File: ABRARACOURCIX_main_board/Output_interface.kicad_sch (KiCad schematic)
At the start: 1 part

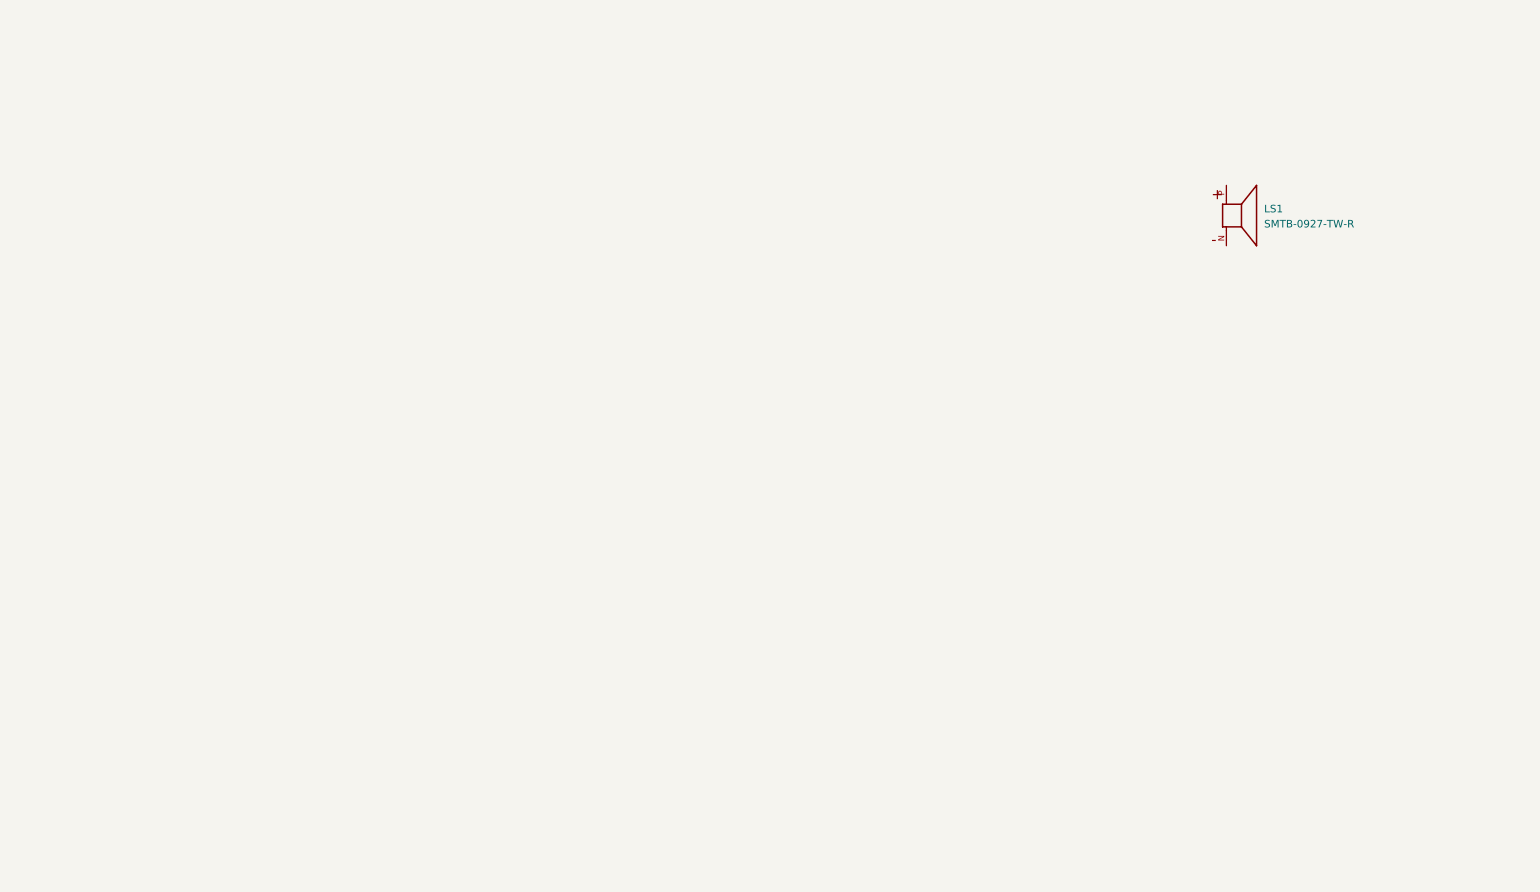
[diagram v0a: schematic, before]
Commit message: Terminé les interconnects
Toutes les interfaces et le power sont terminés. (À vérifier)
Reste à ajouter toutes les connexions au ICM et stm32
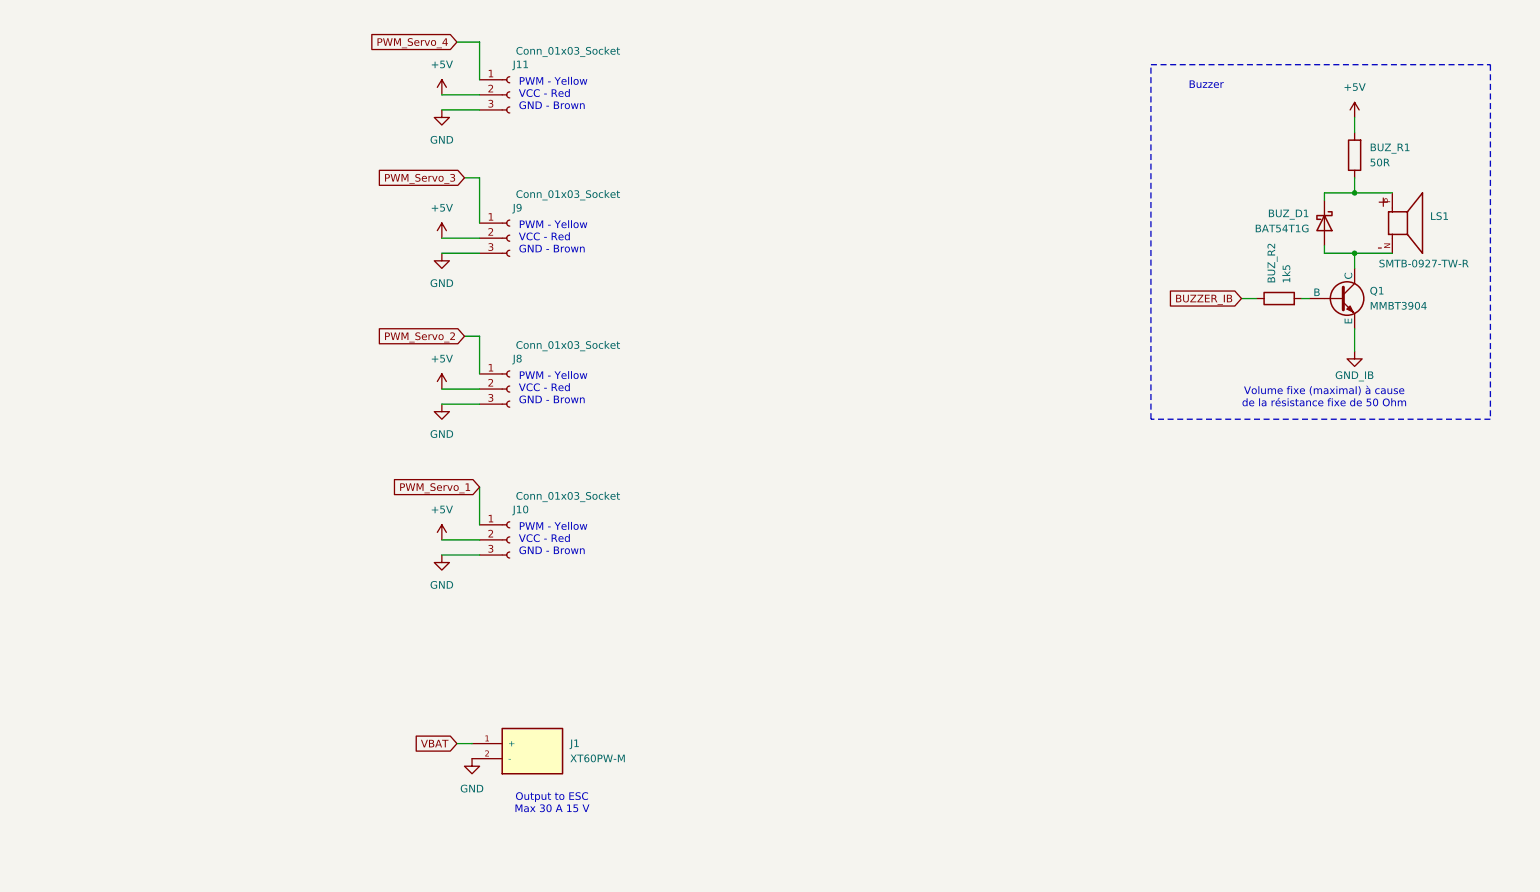
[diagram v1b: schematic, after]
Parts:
- added BUZ_D1: BAT54T1G, Diode_SMD:D_SOD-123, symbol Diode:1N6858UR
- added BUZ_R1: 50R, Resistor_SMD:R_1206_3216Metric, symbol Device:R
- added BUZ_R2: 1k5, Resistor_SMD:R_1206_3216Metric, symbol Device:R
- added J1: XT60PW-M, XT60PW-M:AMASS_XT60PW-M, symbol GAUL_ABRARACOURCIX:XT60PW-M
- added J10, J11, J8, J9: Conn_01x03_Socket, symbol Connector:Conn_01x03_Socket
- added Q1: MMBT3904, Footprints:SOT-23, symbol Simulation_SPICE:NPN
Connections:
- net at LS1.N: now also BUZ_D1.2 (A), Q1.1 (C)
- net at LS1.P: now also BUZ_D1.1 (K), BUZ_R1.1
- new net: BUZ_R2.2, Q1.2 (B)
- new net +5V: BUZ_R1.2, J10.2 (Pin_2), J11.2 (Pin_2), J8.2 (Pin_2), J9.2 (Pin_2)
- new net BUZZER_IB: BUZ_R2.1
- new net GND: J1.2 (-), J10.3 (Pin_3), J11.3 (Pin_3), J8.3 (Pin_3), J9.3 (Pin_3)
- new net GND_IB: Q1.3 (E)
- new net PWM_Servo_1: J10.1 (Pin_1)
- new net PWM_Servo_2: J8.1 (Pin_1)
- new net PWM_Servo_3: J9.1 (Pin_1)
- new net PWM_Servo_4: J11.1 (Pin_1)
- new net VBAT: J1.1 (+)
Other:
- note added: "Buzzer"
- note added: "Output to ESC Max 30 A 15 V"
- note added: "PWM - Yellow VCC - Red GND - Brown"
- note added: "Volume fixe (maximal) à cause de la résistance fixe de 50 Ohm"
- moved on the sheet: LS1

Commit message: Changements obsolete
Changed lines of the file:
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@@
+		)
+	)
+	(rectangle
+		(start 59.69 31.75)
+		(end 116.84 130.81)
+		(stroke
+			(width 0)
+			(type dash)
+		)
+		(fill
+			(type none)
 		)
 	)
@@
 	(wire
 		(pts
+			(xy 83.82 111.76) (xy 83.82 118.11)
+		)
+		(stroke
+			(width 0)
+			(type default)
+		)
+	)
+	(wire
+		(pts
+			(xy 81.28 111.76) (xy 83.82 111.76)
+		)
+		(stroke
+			(width 0)
+			(type default)
+		)
+	)
+	(wire
+		(pts
 			(xy 237.49 72.39) (xy 231.14 72.39)
 		)
@@
 		(pts
 			(xy 212.09 80.01) (xy 214.63 80.01)
-		)
-		(stroke
-			(width 0)
-			(type default)
-		)
-	)
-	(wire
-		(pts
-			(xy 83.82 111.76) (xy 83.82 118.11)
 		)
 		(stroke
@@
 	(global_label "PWM_Servo_1"
 		(shape input)
-		(at 83.82 111.76 180)
+		(at 81.28 111.76 180)
 		(fields_autoplaced yes)
 		(effects
@@
 		)
 		(property "Intersheetrefs" "${INTERSHEET_REFS}"
-			(at 68.3164 111.76 0)
+			(at 65.7764 111.76 0)
 			(effects
 				(font

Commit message: Damn j'ai oublié de push y'a 2 semaines
je sais plus
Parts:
- added C27: C, symbol Device:C
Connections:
- net +5V: now also C27.1
- net GND: now also C27.2
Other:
- note added: "Capacitor sizing: Peak à 0.5 A Rating de courant:"
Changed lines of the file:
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@@
 	)
 	(rectangle
-		(start 59.69 31.75)
+		(start 36.83 31.75)
 		(end 116.84 130.81)
 		(stroke
@@
 			)
 			(justify left)
+		)
+	)
+	(text "Capacitor sizing:\nPeak à 0.5 A\nRating de courant:"
+		(exclude_from_sim no)
+		(at 47.752 56.134 0)
+		(effects
+			(font
+				(size 1.27 1.27)
+			)
 		)
 	)
@@
 	)
 	(symbol
+		(lib_id "power:+5V")
+		(at 44.45 77.47 0)
+		(unit 1)
+		(exclude_from_sim no)
+		(in_bom yes)
+		(on_board yes)
+		(dnp no)
+		(fields_autoplaced yes)
+		(property "Reference" "#PWR045"
+			(at 44.45 81.28 0)
+			(effects
+				(font
+					(size 1.27 1.27)
+				)
+				(hide yes)
+			)
+		)
+		(property "Value" "+5V"
+			(at 44.45 72.39 0)
+			(effects
+				(font
+					(size 1.27 1.27)
+				)
+			)
+		)
+		(property "Footprint" ""
+			(at 44.45 77.47 0)
+			(effects
+				(font
+					(size 1.27 1.27)
+				)
+				(hide yes)
+			)
+		)
+		(property "Datasheet" ""
+			(at 44.45 77.47 0)
+			(effects
+				(font
+					(size 1.27 1.27)
+				)
+				(hide yes)
+			)
+		)
+		(property "Description" "Power symbol creates a global label with name \"+5V\""
+			(at 44.45 77.47 0)
+			(effects
+				(font
+					(size 1.27 1.27)
+				)
+				(hide yes)
+			)
+		)
+		(pin "1"
+		)
+		(instances
+			(project "ABRARACOURCIX_main_board"
+				(path "/0de7b960-2097-47c8-970c-7acab0ada146/f5120b67-a5cd-4c16-9638-751b3f9906f3"
+					(reference "#PWR045")
+					(unit 1)
+				)
+			)
+		)
+	)
+	(symbol
+		(lib_id "power:GND")
+		(at 44.45 85.09 0)
+		(unit 1)
+		(exclude_from_sim no)
+		(in_bom yes)
+		(on_board yes)
+		(dnp no)
+		(fields_autoplaced yes)
+		(property "Reference" "#PWR044"
+			(at 44.45 91.44 0)
+			(effects
+				(font
+					(size 1.27 1.27)
+				)
+				(hide yes)
+			)
+		)
+		(property "Value" "GND"
+			(at 44.45 90.17 0)
+			(effects
+				(font
+					(size 1.27 1.27)
+				)
+			)
+		)
+		(property "Footprint" ""
+			(at 44.45 85.09 0)
+			(effects
+				(font
+					(size 1.27 1.27)
+				)
+				(hide yes)
+			)
+		)
+		(property "Datasheet" ""
+			(at 44.45 85.09 0)
+			(effects
+				(font
+					(size 1.27 1.27)
+				)
+				(hide yes)
+			)
+		)
+		(property "Description" "Power symbol creates a global label with name \"GND\" , ground"
+			(at 44.45 85.09 0)
+			(effects
+				(font
+					(size 1.27 1.27)
+				)
+				(hide yes)
+			)
+		)
+		(pin "1"
+		)
+		(instances
+			(project "ABRARACOURCIX_main_board"
+				(path "/0de7b960-2097-47c8-970c-7acab0ada146/f5120b67-a5cd-4c16-9638-751b3f9906f3"
+					(reference "#PWR044")
+					(unit 1)
+				)
+			)
+		)
+	)
+	(symbol
 		(lib_id "Connector:Conn_01x03_Socket")
 		(at 88.9 95.25 0)
@@
 					(unit 1)
 				)
+			)
+		)
+	)
+	(symbol
+		(lib_id "Device:C")
+		(at 44.45 81.28 0)
+		(unit 1)
+		(exclude_from_sim no)
+		(in_bom yes)
+		(on_board yes)
+		(dnp no)
+		(fields_autoplaced yes)
+		(property "Reference" "C27"
+			(at 48.26 80.0099 0)
+			(effects
+				(font
+					(size 1.27 1.27)
+				)
+				(justify left)
+			)
+		)
+		(property "Value" "C"
+			(at 48.26 82.5499 0)
+			(effects
+				(font
+					(size 1.27 1.27)
+				)
+				(justify left)
+			)
+		)
+		(property "Footprint" ""
+			(at 45.4152 85.09 0)
+			(effects
+				(font
+					(size 1.27 1.27)
+				)
+				(hide yes)
+			)
+		)
+		(property "Datasheet" "~"
+			(at 44.45 81.28 0)
+			(effects
+				(font
+					(size 1.27 1.27)
+				)
+				(hide yes)
+			)
+		)
+		(property "Description" "Unpolarized capacitor"
+			(at 44.45 81.28 0)
+			(effects
+				(font
+					(size 1.27 1.27)
+				)
+				(hide yes)
+			)
+		)
+		(pin "2"
+		)
+		(pin "1"
+		)
+		(instances
+			(project ""
+				(path "/0de7b960-2097-47c8-970c-7acab0ada146/f5120b67-a5cd-4c16-9638-751b3f9906f3"
+					(reference "C27")
+					(unit 1)
+				)

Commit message: Reprise de contrôle
Schematics terminés
Reste à associer des composantes et vérification
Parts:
- added J2: Conn_01x02_Socket, symbol Connector:Conn_01x02_Socket
- C27: value C -> 10u
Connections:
- net GND: now also J2.2 (Pin_2)
- new net PWM_Moteur: J2.1 (Pin_1)
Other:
- note added: "Film capacitor B32522C0106K000 https://www.digikey.ca/en/products/detail/epcos-tdk-electronics/B32522C0106K000/2060953"
- note added: "Motor IO"
- note added: "Output to ESC Max 30 A 15 V XT60 Female"
- note added: "Vérifier cap"
- note removed: "Output to ESC Max 30 A 15 V"
- moved on the sheet: J1

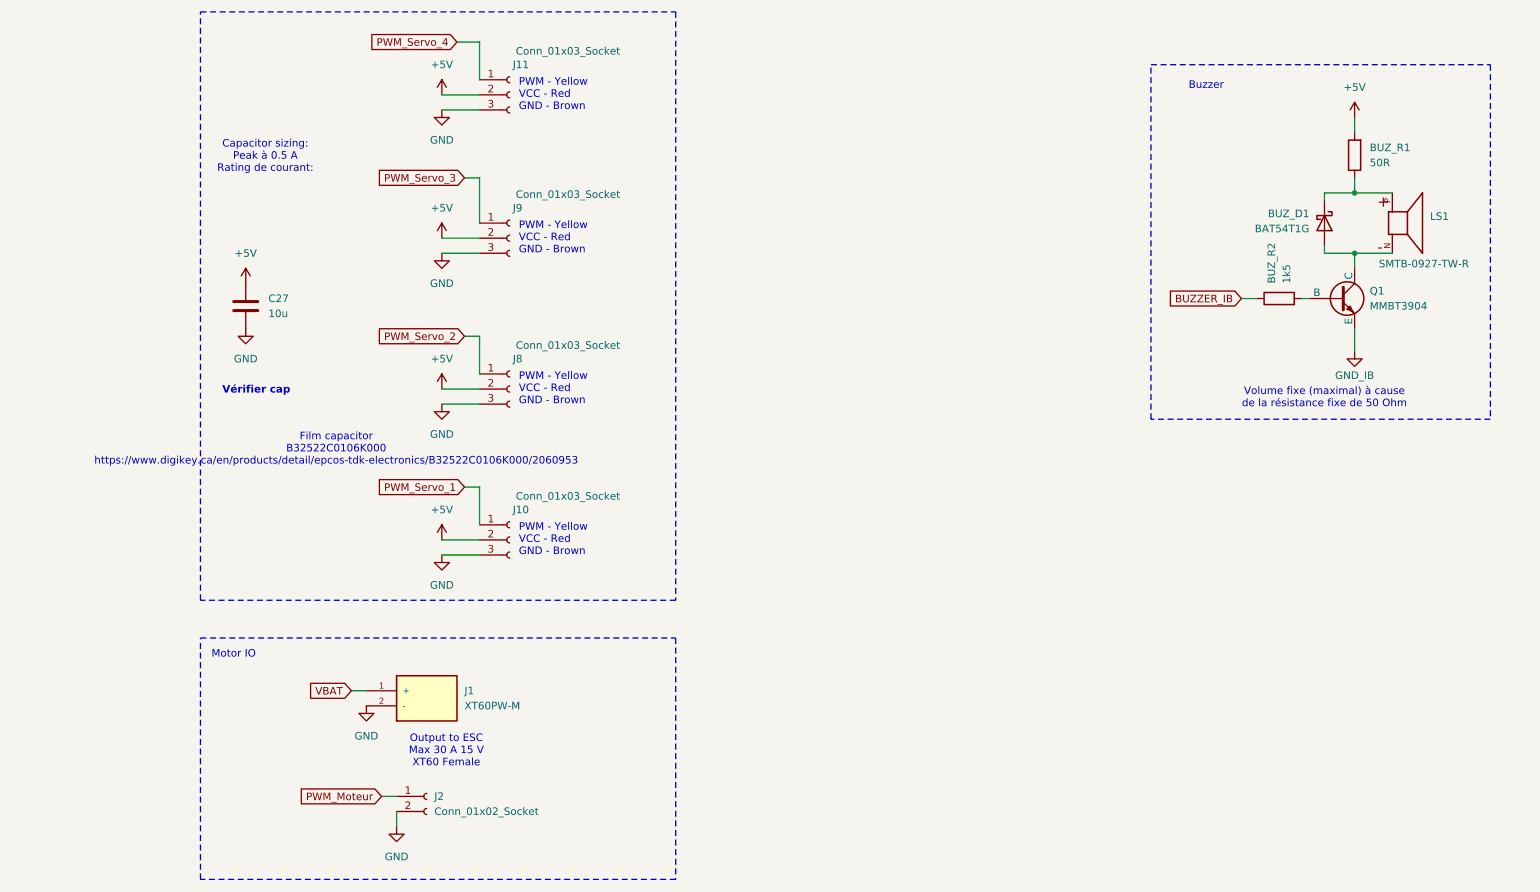
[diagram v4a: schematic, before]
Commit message: Assignation d<empreintes terminée
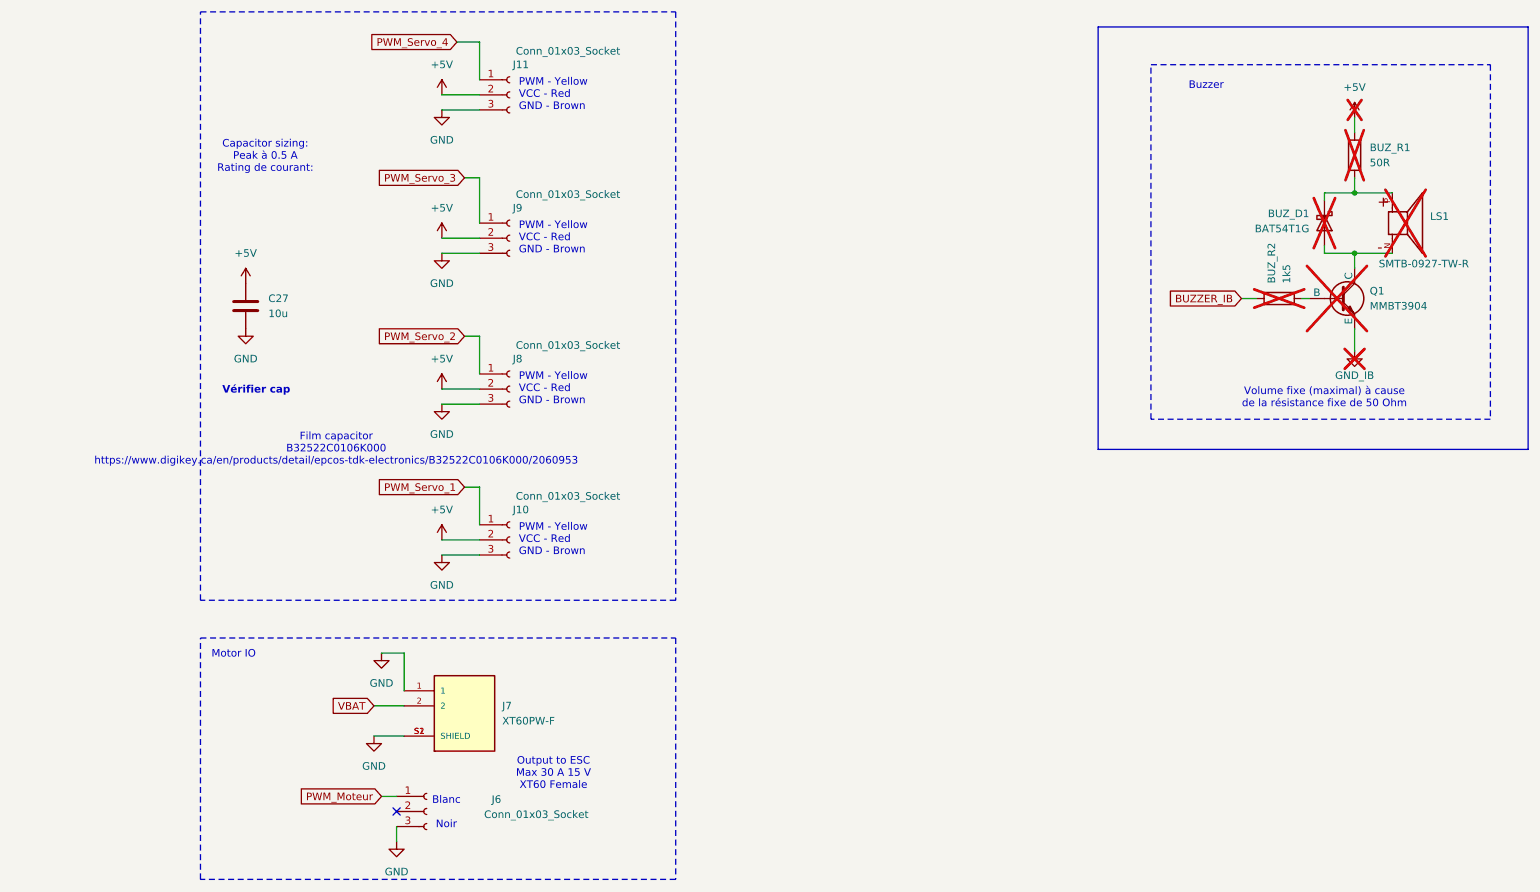
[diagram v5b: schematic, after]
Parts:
- removed J1: XT60PW-M, XT60PW-M:AMASS_XT60PW-M, symbol GAUL_ABRARACOURCIX:XT60PW-M
- removed J2: Conn_01x02_Socket, symbol Connector:Conn_01x02_Socket
- added J6: Conn_01x03_Socket, Connector_PinHeader_2.54mm:PinHeader_1x03_P2.54mm_Horizontal, symbol Connector:Conn_01x03_Socket
- added J7: XT60PW-F, Librairie_footprint:AMASS_XT60PW-F, symbol GAUL_ABRARACOURCIX:XT60PW-F
- BUZ_D1, LS1, Q1: now not fitted; now left out of the parts list
- BUZ_R1, BUZ_R2: footprint Resistor_SMD:R_1206_3216Metric -> Resistor_SMD:R_1206_3216Metric_Pad1.30x1.75mm_HandSolder; now not fitted; now left out of the parts list
- C27: footprint (none) -> Capacitor_SMD:C_1206_3216Metric_Pad1.33x1.80mm_HandSolder
- J10, J11, J8, J9: footprint (none) -> Connector_PinHeader_2.54mm:PinHeader_1x03_P2.54mm_Horizontal
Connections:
- net GND: now also J6.3 (Pin_3), J7.1, J7.S1 (SHIELD), J7.S2 (SHIELD)
- net PWM_Moteur: now also J6.1 (Pin_1)
- net VBAT: now also J7.2
- no-connect marks 0 -> 1
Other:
- note added: "Blanc Noir"
